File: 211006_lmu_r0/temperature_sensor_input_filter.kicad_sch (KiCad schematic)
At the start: 4 parts

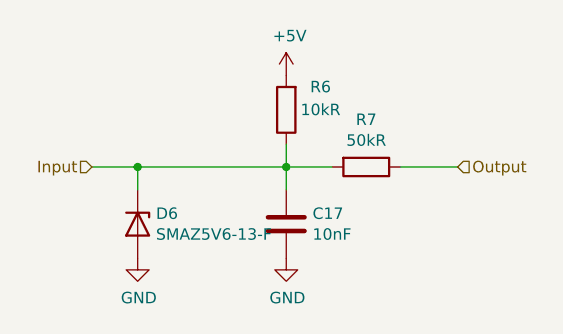
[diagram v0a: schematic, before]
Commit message: fixed footprints for headers, started planning out zones
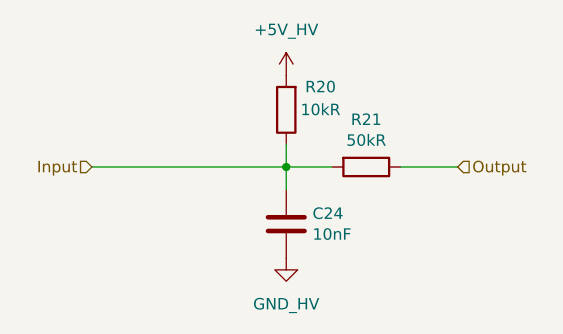
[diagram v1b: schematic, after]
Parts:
- removed D6: SMAZ5V6-13-F, Diode_SMD:D_SMA_Handsoldering, symbol Device:D_Zener
- renumbered C17 to C24, R6 to R20, R7 to R21
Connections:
- net +5V renamed +5V_HV
- net GND renamed GND_HV
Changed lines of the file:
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@@
   (junction (at 158.75 91.44) (diameter 0) (color 0 0 0 0)
-  )
-  (junction (at 142.24 91.44) (diameter 0) (color 0 0 0 0)
   )
   (wire (pts (xy 171.45 91.44) (xy 177.8 91.44))
@@
     (stroke (width 0) (type default) (color 0 0 0 0))
   )
-  (wire (pts (xy 142.24 91.44) (xy 158.75 91.44))
+  (wire (pts (xy 137.16 91.44) (xy 158.75 91.44))
     (stroke (width 0) (type default) (color 0 0 0 0))
   )
@@
     (stroke (width 0) (type default) (color 0 0 0 0))
   )
-  (wire (pts (xy 142.24 91.44) (xy 137.16 91.44))
-    (stroke (width 0) (type default) (color 0 0 0 0))
-  )
   (wire (pts (xy 163.83 91.44) (xy 158.75 91.44))
-    (stroke (width 0) (type default) (color 0 0 0 0))
-  )
-  (wire (pts (xy 142.24 93.98) (xy 142.24 91.44))
     (stroke (width 0) (type default) (color 0 0 0 0))
   )
@@
   (symbol (lib_id "Device:R") (at 167.64 91.44 270)
     (in_bom yes) (on_board yes)
-    (property "Reference" "R7" (id 0) (at 167.64 86.1822 90))
+    (property "Reference" "R21" (id 0) (at 167.64 86.1822 90))
     (property "Value" "50kR" (id 1) (at 167.64 88.4936 90))
     (property "Footprint" "Resistor_SMD:R_0603_1608Metric_Pad0.98x0.95mm_HandSolder" (id 2) (at 167.64 89.662 90)
@@
   (symbol (lib_id "Device:C") (at 158.75 97.79 180)
     (in_bom yes) (on_board yes)
-    (property "Reference" "C17" (id 0) (at 161.671 96.6216 0)
+    (property "Reference" "C24" (id 0) (at 161.671 96.6216 0)
       (effects (font (size 1.27 1.27)) (justify right))
     )
@@
     (pin "2")
   )
-  (symbol (lib_id "power:+5V") (at 158.75 81.28 0)
-    (in_bom yes) (on_board yes)
-    (property "Reference" "#PWR017" (id 0) (at 158.75 85.09 0)
-      (effects (font (size 1.27 1.27)) hide)
-    )
-    (property "Value" "+5V" (id 1) (at 159.131 76.8858 0))
-    (property "Footprint" "" (id 2) (at 158.75 81.28 0)
-      (effects (font (size 1.27 1.27)) hide)
-    )
-    (property "Datasheet" "" (id 3) (at 158.75 81.28 0)
-      (effects (font (size 1.27 1.27)) hide)
-    )
-    (pin "1")
-  )
-  (symbol (lib_id "power:GND") (at 158.75 101.6 0)
-    (in_bom yes) (on_board yes)
-    (property "Reference" "#PWR018" (id 0) (at 158.75 107.95 0)
-      (effects (font (size 1.27 1.27)) hide)
-    )
-    (property "Value" "GND" (id 1) (at 158.877 105.9942 0))
-    (property "Footprint" "" (id 2) (at 158.75 101.6 0)
-      (effects (font (size 1.27 1.27)) hide)
-    )
-    (property "Datasheet" "" (id 3) (at 158.75 101.6 0)
-      (effects (font (size 1.27 1.27)) hide)
-    )
-    (pin "1")
-  )
-  (symbol (lib_id "Device:D_Zener") (at 142.24 97.79 270)
-    (in_bom yes) (on_board yes)
-    (property "Reference" "D6" (id 0) (at 144.272 96.6216 90)
-      (effects (font (size 1.27 1.27)) (justify left))
-    )
-    (property "Value" "SMAZ5V6-13-F" (id 1) (at 144.272 98.933 90)
-      (effects (font (size 1.27 1.27)) (justify left))
-    )
-    (property "Footprint" "Diode_SMD:D_SMA_Handsoldering" (id 2) (at 142.24 97.79 0)
-      (effects (font (size 1.27 1.27)) hide)
-    )
-    (property "Datasheet" "~" (id 3) (at 142.24 97.79 0)
-      (effects (font (size 1.27 1.27)) hide)
-    )
-    (property "Part Number" "SMAZ5V6-13-F" (id 4) (at 142.24 97.79 90)
-      (effects (font (size 1.27 1.27)) hide)
-    )
-    (property "Manufacturer" "Diodes Inc" (id 5) (at 142.24 97.79 90)
-      (effects (font (size 1.27 1.27)) hide)
-    )
-    (property "Mouser Part Number" "NOT AVAILABLE!" (id 6) (at 142.24 97.79 0)
-      (effects (font (size 1.27 1.27)) hide)
-    )
-    (property "Mouser URL" "NOT AVAILABLE!" (id 7) (at 142.24 97.79 0)
-      (effects (font (size 1.27 1.27)) hide)
-    )
-    (pin "1")
-    (pin "2")
-  )
-  (symbol (lib_id "power:GND") (at 142.24 101.6 0)
-    (in_bom yes) (on_board yes)
-    (property "Reference" "#PWR016" (id 0) (at 142.24 107.95 0)
-      (effects (font (size 1.27 1.27)) hide)
-    )
-    (property "Value" "GND" (id 1) (at 142.367 105.9942 0))
-    (property "Footprint" "" (id 2) (at 142.24 101.6 0)
-      (effects (font (size 1.27 1.27)) hide)
-    )
-    (property "Datasheet" "" (id 3) (at 142.24 101.6 0)
-      (effects (font (size 1.27 1.27)) hide)
-    )
-    (pin "1")
-  )
   (symbol (lib_id "Device:R") (at 158.75 85.09 180)
     (in_bom yes) (on_board yes)
-    (property "Reference" "R6" (id 0) (at 162.56 82.55 0))
+    (property "Reference" "R20" (id 0) (at 162.56 82.55 0))
     (property "Value" "10kR" (id 1) (at 162.56 85.09 0))
     (property "Footprint" "Resistor_SMD:R_0603_1608Metric_Pad0.98x0.95mm_HandSolder" (id 2) (at 160.528 85.09 90)
@@
     (pin "2")
   )
+  (symbol (lib_id "gnd_hv:GND_HV") (at 158.75 101.6 0)
+    (in_bom yes) (on_board yes) (fields_autoplaced)
+    (property "Reference" "#PWR0141" (id 0) (at 158.75 107.95 0)
+      (effects (font (size 1.27 1.27)) hide)
+    )
+    (property "Value" "GND_HV" (id 1) (at 158.75 106.68 0))
+    (property "Footprint" "" (id 2) (at 158.75 101.6 0)
+      (effects (font (size 1.27 1.27)) hide)
+    )
+    (property "Datasheet" "" (id 3) (at 158.75 101.6 0)
+      (effects (font (size 1.27 1.27)) hide)
+    )
+    (pin "1")
+  )
+  (symbol (lib_id "+5v_hv:+5V_HV") (at 158.75 81.28 0)
+    (in_bom yes) (on_board yes) (fields_autoplaced)
+    (property "Reference" "#PWR0140" (id 0) (at 158.75 85.09 0)
+      (effects (font (size 1.27 1.27)) hide)
+    )
+    (property "Value" "+5V_HV" (id 1) (at 158.75 76.2 0))
+    (property "Footprint" "" (id 2) (at 158.75 81.28 0)
+      (effects (font (size 1.27 1.27)) hide)
+    )
+    (property "Datasheet" "" (id 3) (at 158.75 81.28 0)
+      (effects (font (size 1.27 1.27)) hide)
+    )
+    (pin "1")
+  )
 )

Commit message: trying out a quick thing, recover
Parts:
- renumbered C24 to C22, R20 to R16, R21 to R17
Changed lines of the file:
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@@
   (symbol (lib_id "Device:R") (at 167.64 91.44 270)
     (in_bom yes) (on_board yes)
-    (property "Reference" "R21" (id 0) (at 167.64 86.1822 90))
+    (property "Reference" "R17" (id 0) (at 167.64 86.1822 90))
     (property "Value" "50kR" (id 1) (at 167.64 88.4936 90))
     (property "Footprint" "Resistor_SMD:R_0603_1608Metric_Pad0.98x0.95mm_HandSolder" (id 2) (at 167.64 89.662 90)
@@
   (symbol (lib_id "Device:C") (at 158.75 97.79 180)
     (in_bom yes) (on_board yes)
-    (property "Reference" "C24" (id 0) (at 161.671 96.6216 0)
+    (property "Reference" "C22" (id 0) (at 161.671 96.6216 0)
       (effects (font (size 1.27 1.27)) (justify right))
     )
@@
   (symbol (lib_id "Device:R") (at 158.75 85.09 180)
     (in_bom yes) (on_board yes)
-    (property "Reference" "R20" (id 0) (at 162.56 82.55 0))
+    (property "Reference" "R16" (id 0) (at 162.56 82.55 0))
     (property "Value" "10kR" (id 1) (at 162.56 85.09 0))
     (property "Footprint" "Resistor_SMD:R_0603_1608Metric_Pad0.98x0.95mm_HandSolder" (id 2) (at 160.528 85.09 90)
@@
   (symbol (lib_id "gnd_hv:GND_HV") (at 158.75 101.6 0)
     (in_bom yes) (on_board yes) (fields_autoplaced)
-    (property "Reference" "#PWR0141" (id 0) (at 158.75 107.95 0)
+    (property "Reference" "#PWR0135" (id 0) (at 158.75 107.95 0)
       (effects (font (size 1.27 1.27)) hide)
     )
@@
   (symbol (lib_id "+5v_hv:+5V_HV") (at 158.75 81.28 0)
     (in_bom yes) (on_board yes) (fields_autoplaced)
-    (property "Reference" "#PWR0140" (id 0) (at 158.75 85.09 0)
+    (property "Reference" "#PWR0134" (id 0) (at 158.75 85.09 0)
       (effects (font (size 1.27 1.27)) hide)
     )

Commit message: copying layout
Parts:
- renumbered C22 to C24, R16 to R20, R17 to R21
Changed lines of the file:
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@@
   (symbol (lib_id "Device:R") (at 167.64 91.44 270)
     (in_bom yes) (on_board yes)
-    (property "Reference" "R17" (id 0) (at 167.64 86.1822 90))
+    (property "Reference" "R21" (id 0) (at 167.64 86.1822 90))
     (property "Value" "50kR" (id 1) (at 167.64 88.4936 90))
     (property "Footprint" "Resistor_SMD:R_0603_1608Metric_Pad0.98x0.95mm_HandSolder" (id 2) (at 167.64 89.662 90)
@@
   (symbol (lib_id "Device:C") (at 158.75 97.79 180)
     (in_bom yes) (on_board yes)
-    (property "Reference" "C22" (id 0) (at 161.671 96.6216 0)
+    (property "Reference" "C24" (id 0) (at 161.671 96.6216 0)
       (effects (font (size 1.27 1.27)) (justify right))
     )
@@
   (symbol (lib_id "Device:R") (at 158.75 85.09 180)
     (in_bom yes) (on_board yes)
-    (property "Reference" "R16" (id 0) (at 162.56 82.55 0))
+    (property "Reference" "R20" (id 0) (at 162.56 82.55 0))
     (property "Value" "10kR" (id 1) (at 162.56 85.09 0))
     (property "Footprint" "Resistor_SMD:R_0603_1608Metric_Pad0.98x0.95mm_HandSolder" (id 2) (at 160.528 85.09 90)
@@
   (symbol (lib_id "gnd_hv:GND_HV") (at 158.75 101.6 0)
     (in_bom yes) (on_board yes) (fields_autoplaced)
-    (property "Reference" "#PWR0135" (id 0) (at 158.75 107.95 0)
+    (property "Reference" "#PWR0141" (id 0) (at 158.75 107.95 0)
       (effects (font (size 1.27 1.27)) hide)
     )
@@
   (symbol (lib_id "+5v_hv:+5V_HV") (at 158.75 81.28 0)
     (in_bom yes) (on_board yes) (fields_autoplaced)
-    (property "Reference" "#PWR0134" (id 0) (at 158.75 85.09 0)
+    (property "Reference" "#PWR0140" (id 0) (at 158.75 85.09 0)
       (effects (font (size 1.27 1.27)) hide)
     )

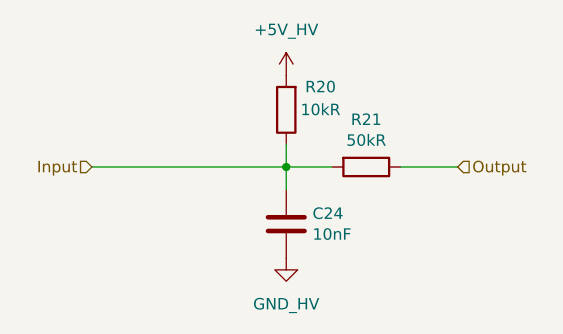
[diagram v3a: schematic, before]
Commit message: going to bulk edit fields
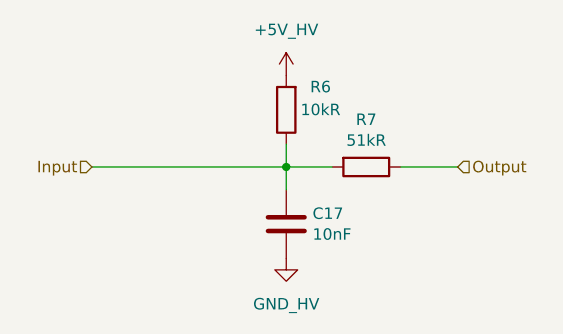
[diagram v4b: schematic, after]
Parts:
- R7: renamed from R21; value 50kR -> 51kR
- renumbered C24 to C17, R20 to R6
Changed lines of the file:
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@@
   (symbol (lib_id "Device:R") (at 167.64 91.44 270)
     (in_bom yes) (on_board yes)
-    (property "Reference" "R21" (id 0) (at 167.64 86.1822 90))
-    (property "Value" "50kR" (id 1) (at 167.64 88.4936 90))
+    (property "Reference" "R7" (id 0) (at 167.64 86.1822 90))
+    (property "Value" "51kR" (id 1) (at 167.64 88.4936 90))
     (property "Footprint" "Resistor_SMD:R_0603_1608Metric_Pad0.98x0.95mm_HandSolder" (id 2) (at 167.64 89.662 90)
       (effects (font (size 1.27 1.27)) hide)
@@
   (symbol (lib_id "Device:C") (at 158.75 97.79 180)
     (in_bom yes) (on_board yes)
-    (property "Reference" "C24" (id 0) (at 161.671 96.6216 0)
+    (property "Reference" "C17" (id 0) (at 161.671 96.6216 0)
       (effects (font (size 1.27 1.27)) (justify right))
     )
@@
   (symbol (lib_id "Device:R") (at 158.75 85.09 180)
     (in_bom yes) (on_board yes)
-    (property "Reference" "R20" (id 0) (at 162.56 82.55 0))
+    (property "Reference" "R6" (id 0) (at 162.56 82.55 0))
     (property "Value" "10kR" (id 1) (at 162.56 85.09 0))
     (property "Footprint" "Resistor_SMD:R_0603_1608Metric_Pad0.98x0.95mm_HandSolder" (id 2) (at 160.528 85.09 90)

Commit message: started to export and fix things
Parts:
- renumbered C17 to C24, R6 to R20, R7 to R21
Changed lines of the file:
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@@
   (symbol (lib_id "Device:R") (at 167.64 91.44 270)
     (in_bom yes) (on_board yes)
-    (property "Reference" "R7" (id 0) (at 167.64 86.1822 90))
+    (property "Reference" "R21" (id 0) (at 167.64 86.1822 90))
     (property "Value" "51kR" (id 1) (at 167.64 88.4936 90))
     (property "Footprint" "Resistor_SMD:R_0603_1608Metric_Pad0.98x0.95mm_HandSolder" (id 2) (at 167.64 89.662 90)
@@
   (symbol (lib_id "Device:C") (at 158.75 97.79 180)
     (in_bom yes) (on_board yes)
-    (property "Reference" "C17" (id 0) (at 161.671 96.6216 0)
+    (property "Reference" "C24" (id 0) (at 161.671 96.6216 0)
       (effects (font (size 1.27 1.27)) (justify right))
     )
@@
   (symbol (lib_id "Device:R") (at 158.75 85.09 180)
     (in_bom yes) (on_board yes)
-    (property "Reference" "R6" (id 0) (at 162.56 82.55 0))
+    (property "Reference" "R20" (id 0) (at 162.56 82.55 0))
     (property "Value" "10kR" (id 1) (at 162.56 85.09 0))
     (property "Footprint" "Resistor_SMD:R_0603_1608Metric_Pad0.98x0.95mm_HandSolder" (id 2) (at 160.528 85.09 90)
